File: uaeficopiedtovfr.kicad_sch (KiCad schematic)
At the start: 37 parts, among them J1 DTF13-12PB, J1 USB_B_Mini, J1 USB_C_Receptacle_USB2.0, J17 Conn_01x06, J4 DTF13-12PB, J5 Conn_01x05_Male, M1 Module-power_12and5V-0.2, M3 Module-knock-0.2, M3 Module-vr-discrete-0.4, M4 Module-vr-max9924-0.1, M5 Module-wbo-0.5, M6 Module:mega-mcu100/0.2, M7 Module-wbo-0.5, M8 Module-sd-0.1, P1 Pad, P2 Pad, P3 Pad, P4 Pad, U4 JDY-33

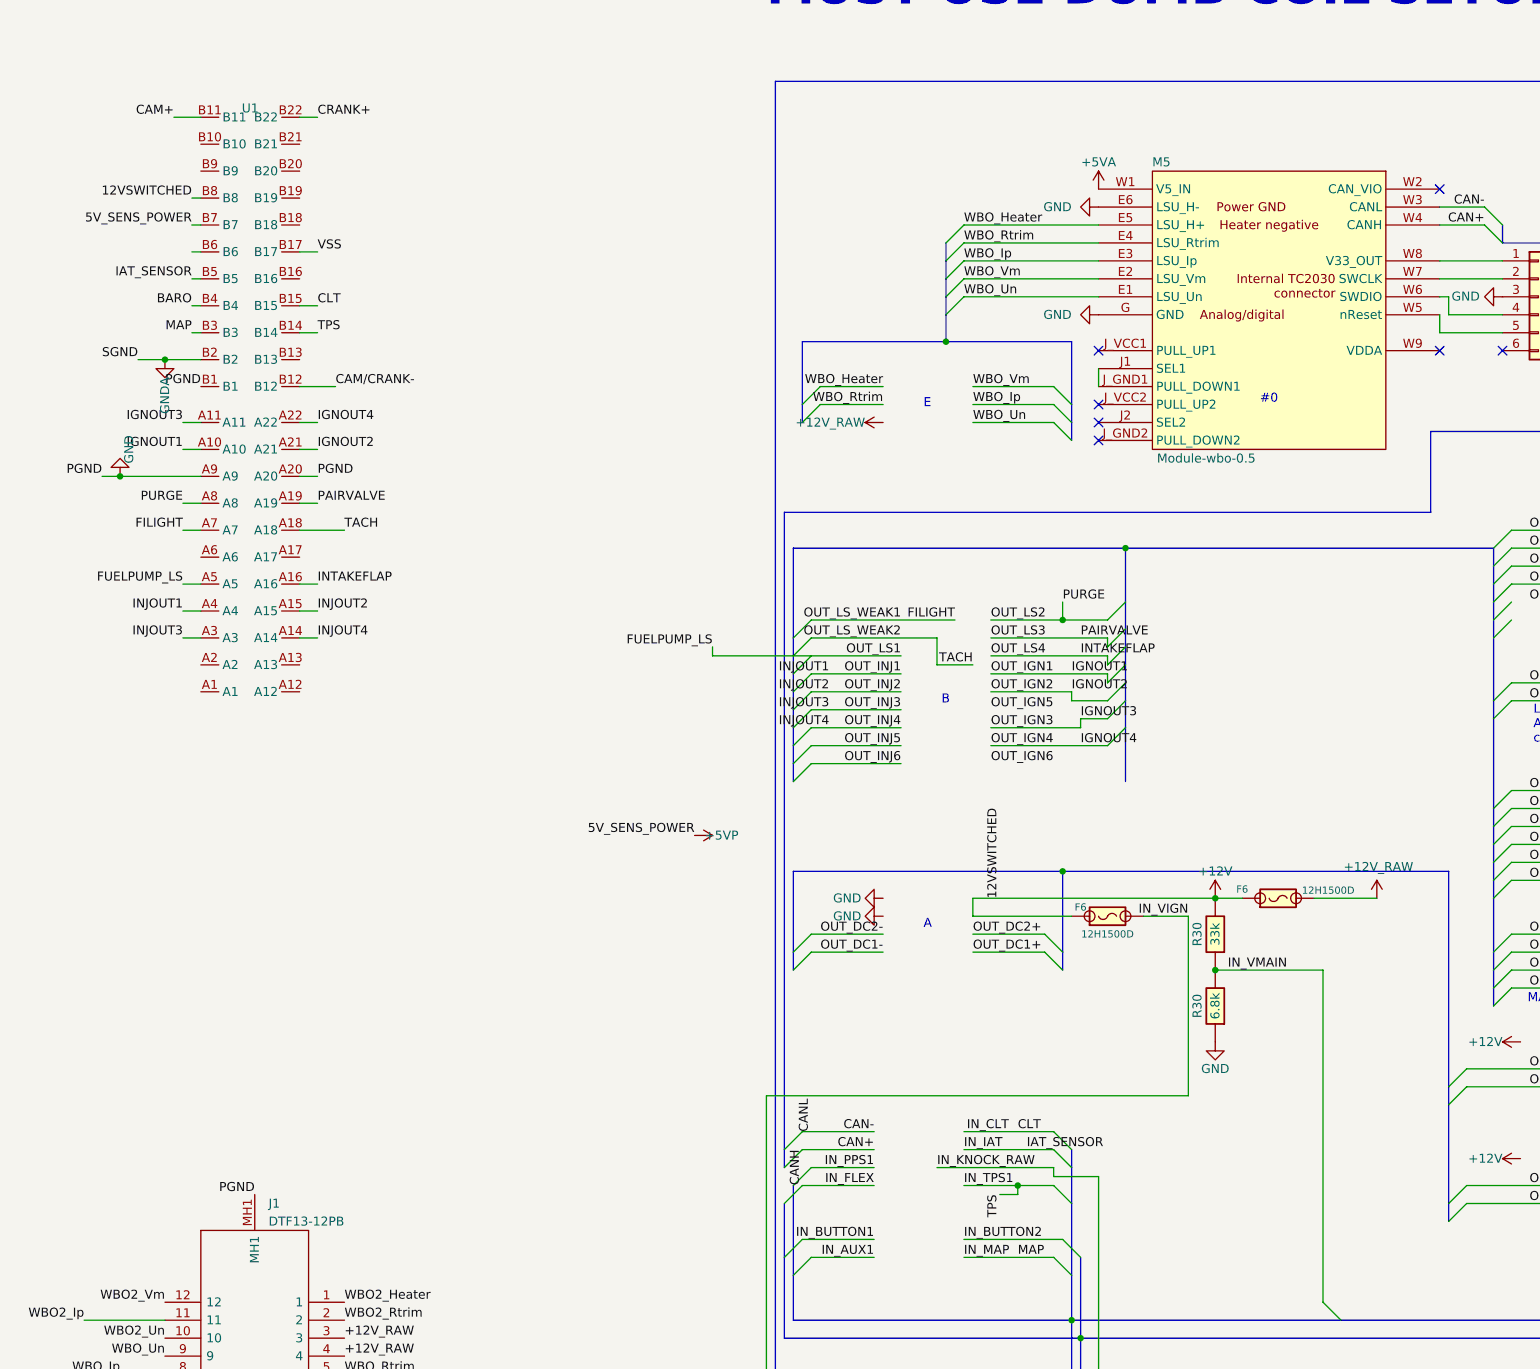
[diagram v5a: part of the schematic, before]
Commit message: Routed B10 and B21 to button inputs 1 and 2
These have something to do with killing the engine if you put it in gear with the kickstand down or try to start it in gear with the kickstand down
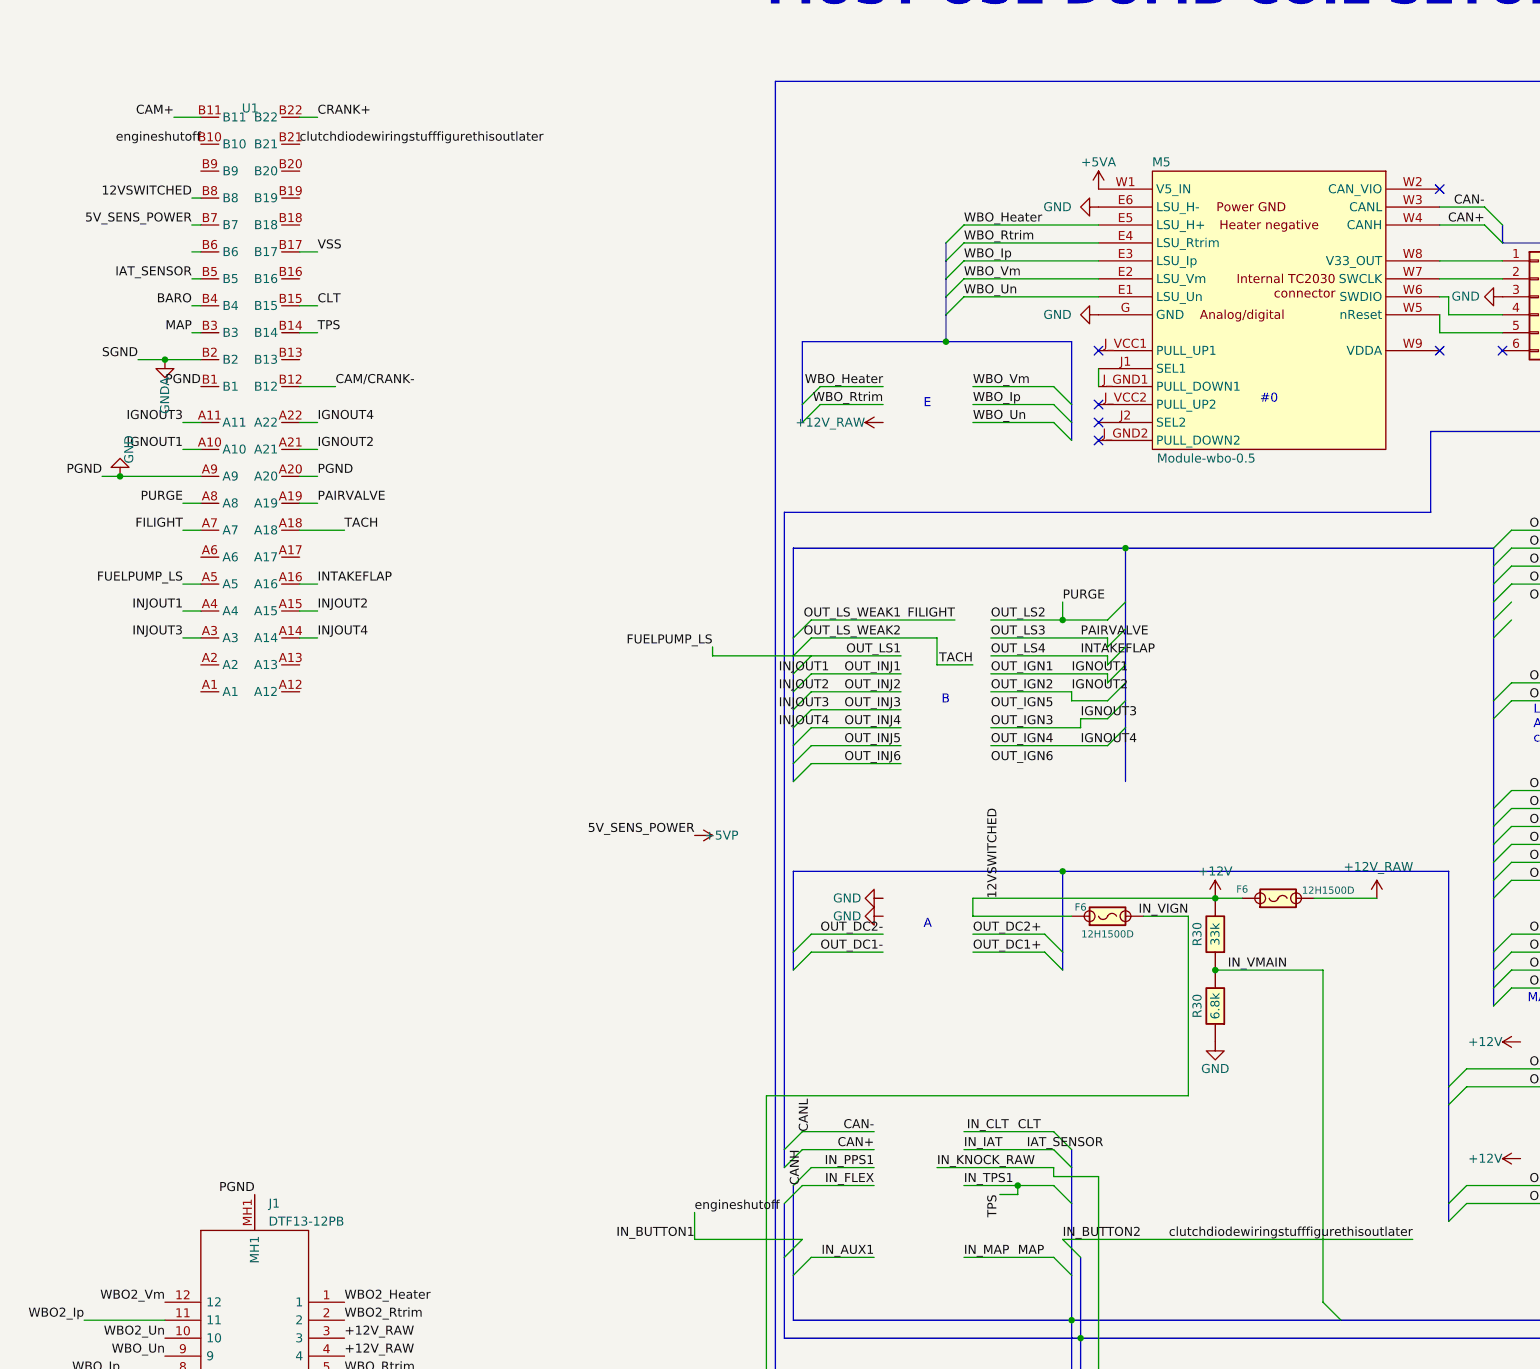
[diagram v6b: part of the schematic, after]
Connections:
- net IN_BUTTON1: now also U1.B10
- net IN_BUTTON2: now also U1.B21
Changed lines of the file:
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@@
     (stroke (width 0) (type solid))
-  )
-  (wire (pts (xy 110.49 196.85) (xy 120.65 196.85))
-    (stroke (width 0) (type default))
   )
   (bus (pts (xy 109.22 111.76) (xy 109.22 114.3))
@@
     (stroke (width 0) (type default) (color 194 194 0 1))
   )
+  (wire (pts (xy 95.25 193.04) (xy 95.25 196.85))
+    (stroke (width 0) (type default))
+  )
   (wire (pts (xy 142.24 226.06) (xy 142.24 229.87))
     (stroke (width 0) (type default))
@@
     (stroke (width 0) (type solid))
   )
-  (wire (pts (xy 133.35 196.85) (xy 147.32 196.85))
+  (wire (pts (xy 196.85 196.85) (xy 147.32 196.85))
     (stroke (width 0) (type default))
   )
@@
     (stroke (width 0) (type default))
   )
+  (wire (pts (xy 95.25 196.85) (xy 110.49 196.85))
+    (stroke (width 0) (type default))
+  )
   (wire (pts (xy 156.21 229.87) (xy 170.18 229.87))
     (stroke (width 0) (type default))
@@
     (effects (font (size 1.27 1.27)) (justify right bottom))
   )
+  (label "engineshutoff" (at 95.25 193.04 0) (fields_autoplaced)
+    (effects (font (size 1.27 1.27)) (justify left bottom))
+  )
   (label "INJOUT1" (at 22.86 107.95 180) (fields_autoplaced)
     (effects (font (size 1.27 1.27)) (justify right bottom))
@@
     (effects (font (size 1.27 1.27)) (justify right bottom))
   )
-  (label "IN_BUTTON1" (at 120.65 196.85 180) (fields_autoplaced)
+  (label "IN_BUTTON1" (at 95.25 196.85 180) (fields_autoplaced)
     (effects (font (size 1.27 1.27)) (justify right bottom))
   )
@@
     (effects (font (size 1.27 1.27)) (justify left bottom))
   )
+  (label "clutchdiodewiringstufffigurethisoutlater" (at 196.85 196.85 180) (fields_autoplaced)
+    (effects (font (size 1.27 1.27)) (justify right bottom))
+  )
   (label "VREF1" (at 260.35 252.73 0) (fields_autoplaced)
     (effects (font (size 1.27 1.27)) (justify left bottom))
@@
     (effects (font (size 1.27 1.27)) (justify left bottom))
   )
-  (label "IN_BUTTON2" (at 133.35 196.85 0) (fields_autoplaced)
+  (label "IN_BUTTON2" (at 147.32 196.85 0) (fields_autoplaced)
     (effects (font (size 1.27 1.27)) (justify left bottom))
   )
@@
     (effects (font (size 1.27 1.27)) (justify right bottom))
   )
+  (label "engineshutoff" (at 25.4 41.91 180) (fields_autoplaced)
+    (effects (font (size 1.27 1.27)) (justify right bottom))
+  )
   (label "IN_IAT" (at 133.35 184.15 0) (fields_autoplaced)
     (effects (font (size 1.27 1.27)) (justify left bottom))
@@
     (effects (font (size 1.27 1.27)) (justify right bottom))
   )
+  (label "clutchdiodewiringstufffigurethisoutlater" (at 39.37 41.91 0) (fields_autoplaced)
+    (effects (font (size 1.27 1.27)) (justify left bottom))
+  )
   (label "IGNOUT2" (at 148.59 119.38 0) (fields_autoplaced)

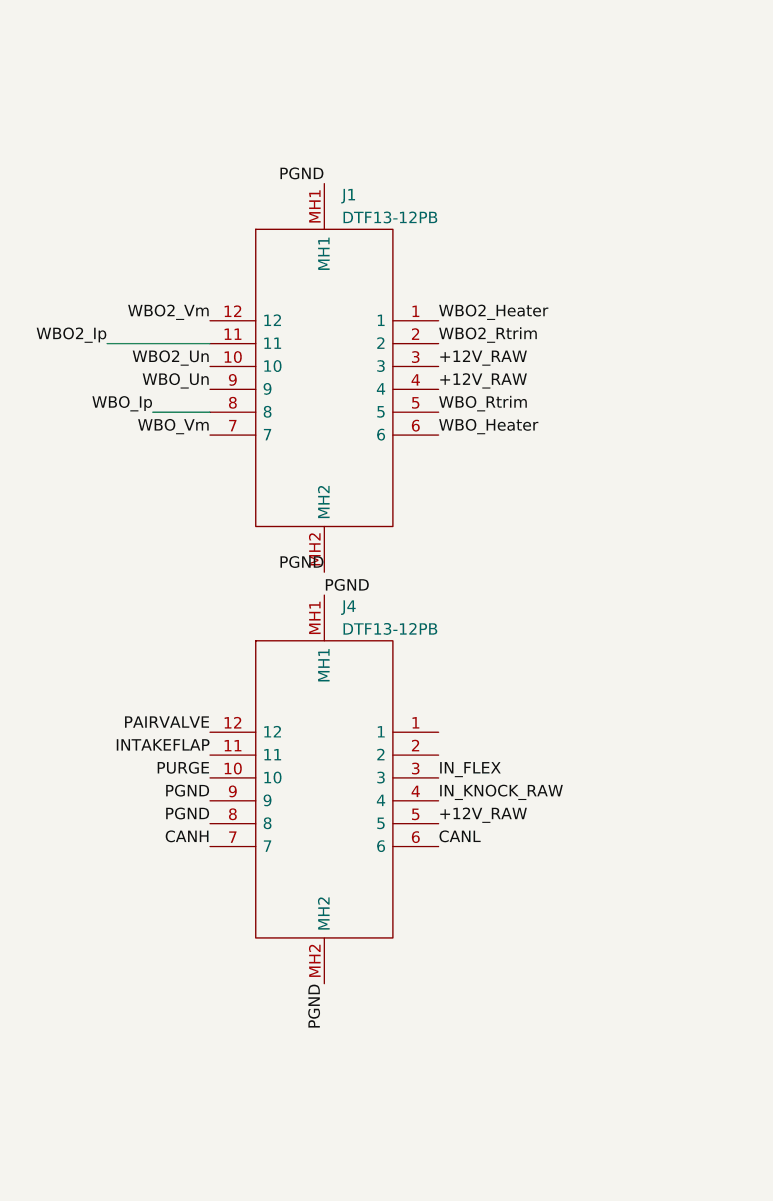
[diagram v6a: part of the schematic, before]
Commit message: Changed two deutsch connectors to single ampseal
I did some fitment tests and decided a single big connector dead center in the board will fit the best
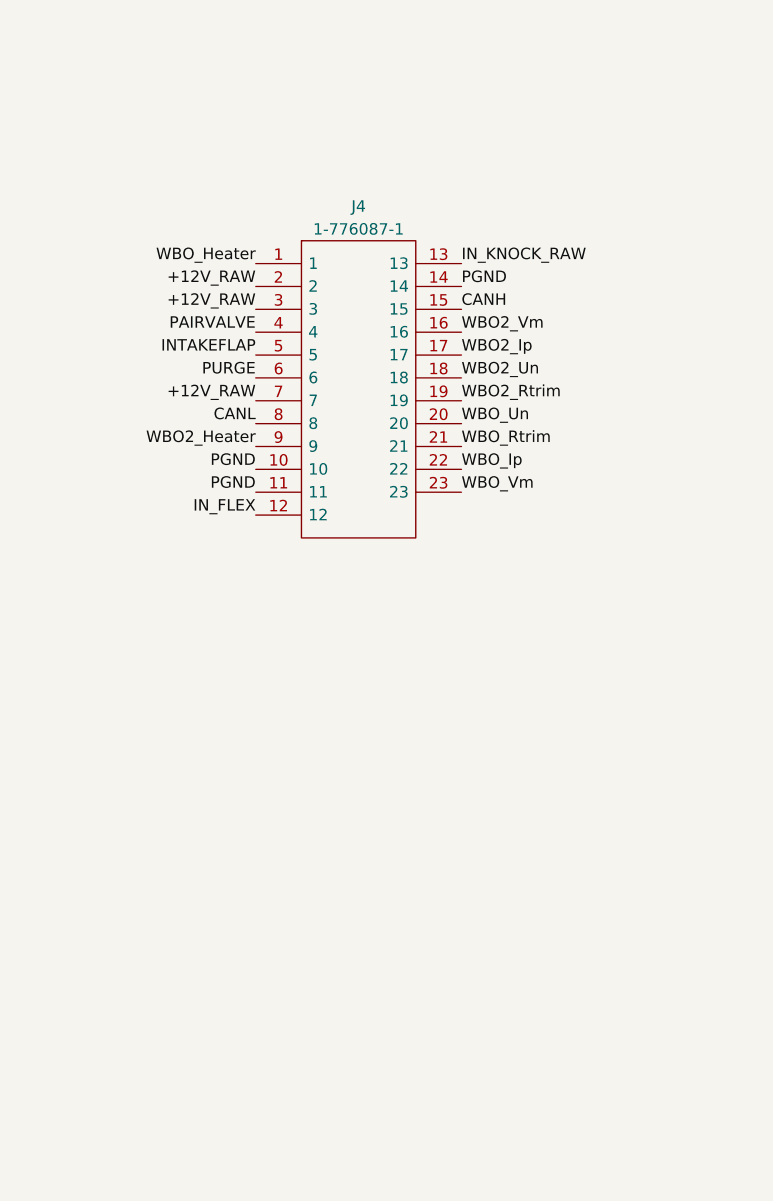
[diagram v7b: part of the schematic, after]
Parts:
- removed J1, J4: DTF13-12PB, DTF1312PB, symbol SamacSys_Parts:DTF13-12PB
- added J4: 1-776087-1, 17760871, symbol SamacSys_Parts:1-776087-1
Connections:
- net +12V_RAW: now also J4.2, J4.3, J4.7
- net CAN+: now also J4.15
- net CAN-: now also J4.8
- net GND: now also J4.10, J4.11, J4.14
- net INTAKEFLAP: now also J4.5
- net IN_FLEX: now also J4.12
- net IN_KNOCK_RAW: now also J4.13
- net OUT_LS2: now also J4.6
- net OUT_LS3: now also J4.4
- net WBO2_Heater: now also J4.9
- net WBO2_Ip: now also J4.17
- net WBO2_Rtrim: now also J4.19
- net WBO2_Un: now also J4.18
- net WBO2_Vm: now also J4.16
- net WBO_Heater: now also J4.1
- net WBO_Ip: now also J4.22
- net WBO_Rtrim: now also J4.21
- net WBO_Un: now also J4.20
- net WBO_Vm: now also J4.23
